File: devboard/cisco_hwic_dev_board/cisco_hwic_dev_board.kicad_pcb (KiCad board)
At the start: 2 copper layers, 3 parts, among them J1 Conn_02x20_Odd_Even, J2 Conn_02x34_Top_Bottom_Cisco, J3 Conn_01x15

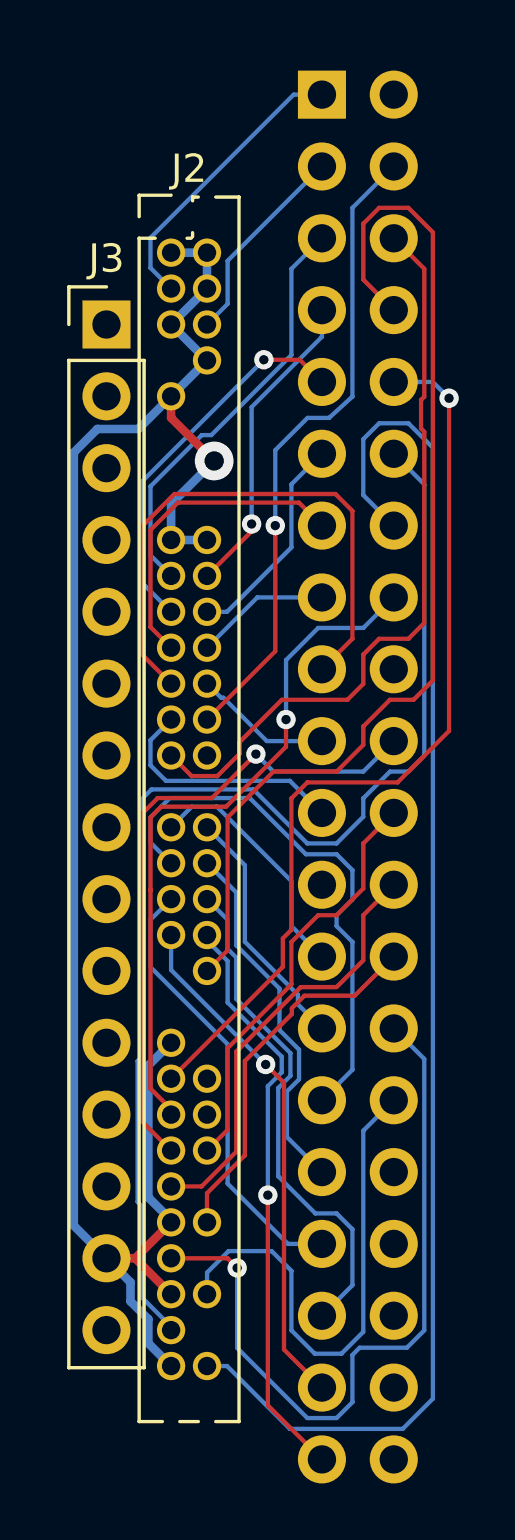
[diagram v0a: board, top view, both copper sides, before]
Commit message: Expansion connector routed.
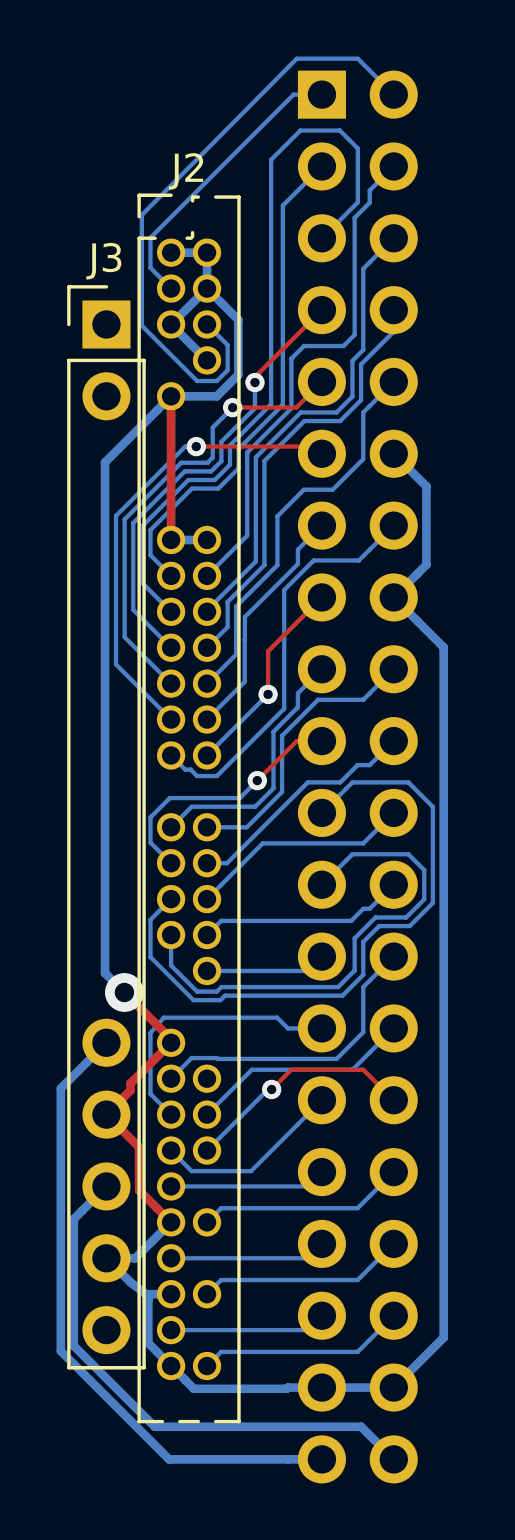
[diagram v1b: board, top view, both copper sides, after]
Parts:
- J3: footprint Connector_PinHeader_2.54mm:PinHeader_1x15_P2.54mm_Vertical -> cisco_hwic_dev_board:PinHeader_1x15_P2.54mm_Vertical_Cisco
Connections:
- J1 pad 10: /DCLK_OE_ -> /PB7
- J1 pad 11: /PB3 -> /PB8
- J1 pad 12: /PH0 -> GND
- J1 pad 13: /PB4 -> /PC0
- J1 pad 14: /PH1 -> /PC1
- J1 pad 15: /PB5 -> /PC2
- J1 pad 16: /PG0 -> GND
- J1 pad 17: /PB6 -> /PD0
- J1 pad 18: /PG1 -> /PD1
- J1 pad 19: /PB7 -> /PD2
- J1 pad 2: Net-(J1-Pad2) -> /PA1
- J1 pad 20: /PG2 -> /PD3
- J1 pad 21: /PB8 -> /PD4
- J1 pad 22: /PG3 -> /PD5
- J1 pad 23: Net-(J1-Pad23) -> /PD6
- J1 pad 24: /PG4 -> /PD7
- J1 pad 25: /PD0 -> /PE0
- J1 pad 26: /PG5 -> /DCLK_OE_
- J1 pad 27: /PD1 -> /PG0
- J1 pad 28: /PG6 -> /PG1
- J1 pad 29: /PD2 -> /PG2
- J1 pad 3: /PA1 -> /DATA0
- J1 pad 30: /PG7 -> /PG3
- J1 pad 31: /PD3 -> /PG4
- J1 pad 32: Net-(J1-Pad32) -> /PG5
- J1 pad 33: /PD4 -> /PG6
- J1 pad 34: Net-(J1-Pad34) -> /PG7
- J1 pad 35: /PD5 -> /PH0
- J1 pad 36: Net-(J1-Pad36) -> /PH1
- J1 pad 37: /PD6 -> GND
- J1 pad 38: Net-(J1-Pad38) -> GND
- J1 pad 39: /PD7 -> +5V
- J1 pad 4: /PC0 -> /PB1
- J1 pad 40: Net-(J1-Pad40) -> +3V3
- J1 pad 5: /DATA0 -> /PB2
- J1 pad 6: /PC1 -> /PB3
- J1 pad 7: /PB1 -> /PB4
- J1 pad 8: /PE0 -> /PB5
- J1 pad 9: /PB2 -> /PB6
- J2 pad 50: /Pin_50 -> /PC2
- J2 pad 60: Net-(J2-Pad60) -> /PG1
- J3 pad 11: Net-(J3-Pad11) -> +5V
- J3 pad 12: +5V -> GND
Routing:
- net /PH1: track 49.5 -> 7.34 mm
- net GND: track 65.2 -> 103.9 mm
- net /PH0: track 43.0 -> 5.54 mm
- net /PE0: track 37.8 -> 4.27 mm
- net +5V: track 0.00 -> 22.4 mm
- net /DCLK_OE_: track 32.2 -> 10.6 mm, vias 1 -> 0
- net /PG6: track 26.3 -> 5.54 mm, vias 1 -> 0
- net +3V3: track 0.00 -> 19.1 mm
- net /PG2: track 22.8 -> 6.67 mm, vias 1 -> 0
- net /PG0: track 24.5 -> 9.66 mm, vias 1 -> 0
- net /PA1: track 7.27 -> 21.6 mm
- net /PC0: track 22.8 -> 8.54 mm, vias 1 -> 0
- net /PD7: track 20.6 -> 7.34 mm, vias 1 -> 0
- net /PB2: track 13.5 -> 26.3 mm, vias 1 -> 0
- net /PC1: track 26.5 -> 14.3 mm
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
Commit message: First version.
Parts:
- added C1: C, Capacitor_SMD:C_0603_1608Metric_Pad1.05x0.95mm_HandSolder, F.Cu at (-551.3, -538.7)
- added C2: C, Capacitor_SMD:C_0603_1608Metric_Pad1.05x0.95mm_HandSolder, F.Cu at (-547.0, -564.4)
- added J4: USB Blaster Active Serial, Connector_PinHeader_2.54mm:PinHeader_2x05_P2.54mm_Vertical, B.Cu at (-551.9, -550.7)
- added J5: ATT85_VIN, Connector_PinHeader_2.54mm:PinHeader_1x01_P2.54mm_Vertical, B.Cu at (-554.5, -566.2)
- added J6: SD Card, Connector_PinHeader_2.54mm:PinHeader_1x06_P2.54mm_Vertical, B.Cu at (-554.5, -536.4)
- added J7: Power, Connector_PinHeader_2.54mm:PinHeader_1x03_P2.54mm_Horizontal, F.Cu at (-554.2, -579.6)
- added JP1: 3.3V Main, Connector_PinHeader_2.54mm:PinHeader_2x01_P2.54mm_Vertical, B.Cu at (-554.5, -561.8)
- added JP2: Jumper_3_Bridged12, Connector_PinHeader_2.54mm:PinHeader_1x03_P2.54mm_Vertical, B.Cu at (-554.2, -555.8)
- added R3: NS, Resistor_SMD:R_0603_1608Metric_Pad1.05x0.95mm_HandSolder, F.Cu at (-549.0, -578.6)
- added R4: NS, Resistor_SMD:R_0603_1608Metric_Pad1.05x0.95mm_HandSolder, F.Cu at (-545.5, -578.6)
- added R5: NS, Resistor_SMD:R_0603_1608Metric_Pad1.05x0.95mm_HandSolder, F.Cu at (-549.0, -580.1)
- added R6: NS, Resistor_SMD:R_0603_1608Metric_Pad1.05x0.95mm_HandSolder, F.Cu at (-545.5, -580.1)
- added R7: NS, Resistor_SMD:R_0603_1608Metric_Pad1.05x0.95mm_HandSolder, F.Cu at (-550.8, -581.9)
- added R8: NS, Resistor_SMD:R_0603_1608Metric_Pad1.05x0.95mm_HandSolder, F.Cu at (-545.5, -581.9)
- added U1: AT25xxx, Package_SO:SOIC-8_3.9x4.9mm_P1.27mm, F.Cu at (-548.5, -569.3)
- added U2: ATtiny85_devboard, cisco_hwic_dev_board:Digispark_ATtiny85, B.Cu at (-551.7, -584.7)
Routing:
- net GND: track 103.9 -> 211.8 mm, vias 1 -> 3
- net +3V3: track 19.1 -> 109.5 mm, vias 0 -> 2
- net /DCLK: track 0.00 -> 71.0 mm, vias 0 -> 3
- net /DATA0: track 17.8 -> 77.2 mm, vias 0 -> 2
- net /SPI_MISO: track 0.00 -> 58.3 mm, vias 0 -> 1
- net /DCLK_OE_: track 10.6 -> 64.9 mm
- net +5V: track 22.4 -> 73.9 mm
- net /SPISD_CSN: track 0.00 -> 32.2 mm
- net /PC1: track 14.3 -> 41.1 mm
- net /SPI_CSN: track 0.00 -> 26.4 mm
- net /PC0: track 8.54 -> 34.6 mm, vias 0 -> 2
- net /SD_CSN: track 0.00 -> 22.1 mm
- net Net-(J5-Pad1): track 0.00 -> 12.3 mm
- net Net-(JP1-Pad1): track 0.00 -> 11.0 mm
- net Net-(R8-Pad2): track 0.00 -> 6.77 mm
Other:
- board outline added: 27.4 x 52.1 mm
- board text added: "3.3V"
- board text added: "5V"
- board text added: "DCLK"
- board text added: "GND"
- board text added: "MISO"
- board text added: "MOSI"
- board text added: "PA0"
- board text added: "PB0"
- board text added: "PC0"
- board text added: "PD0"
- board text added: "PE0"
- board text added: "PG0"
- board text added: "PH0"

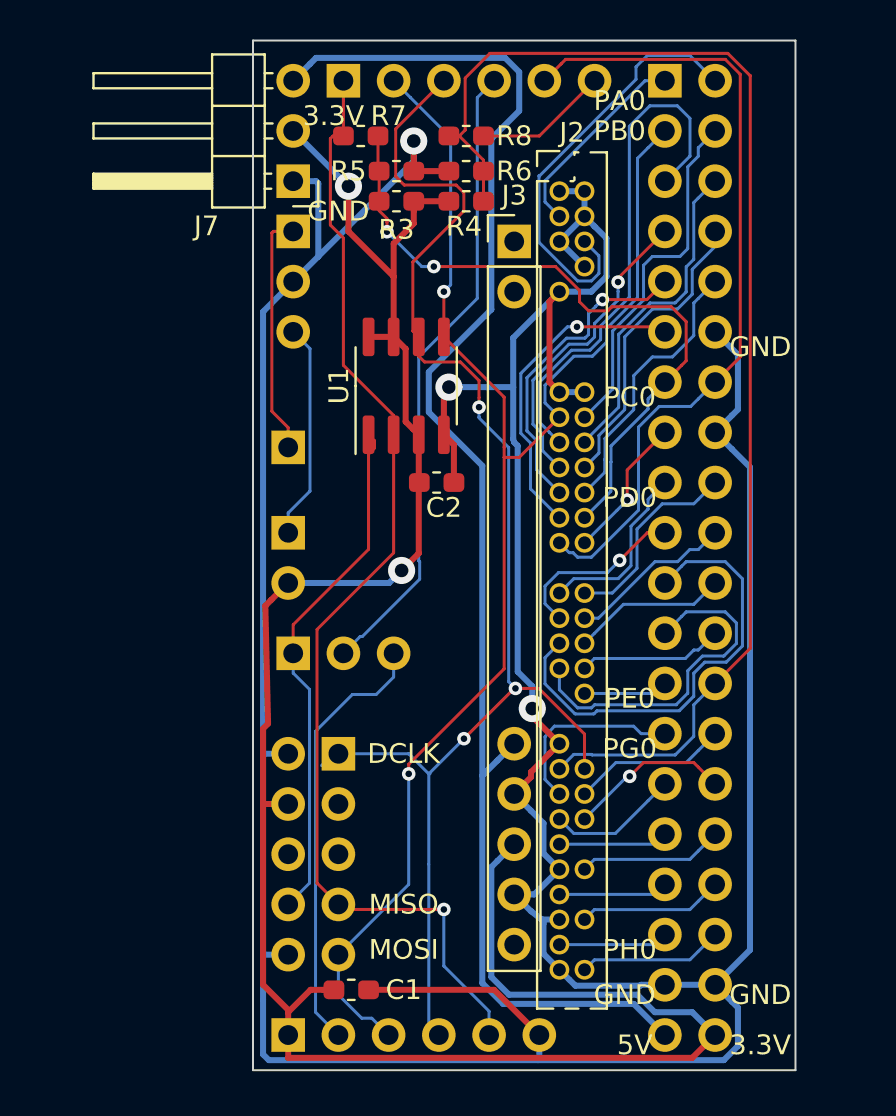
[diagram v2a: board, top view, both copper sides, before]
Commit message: Various fixes after broken rev 1.
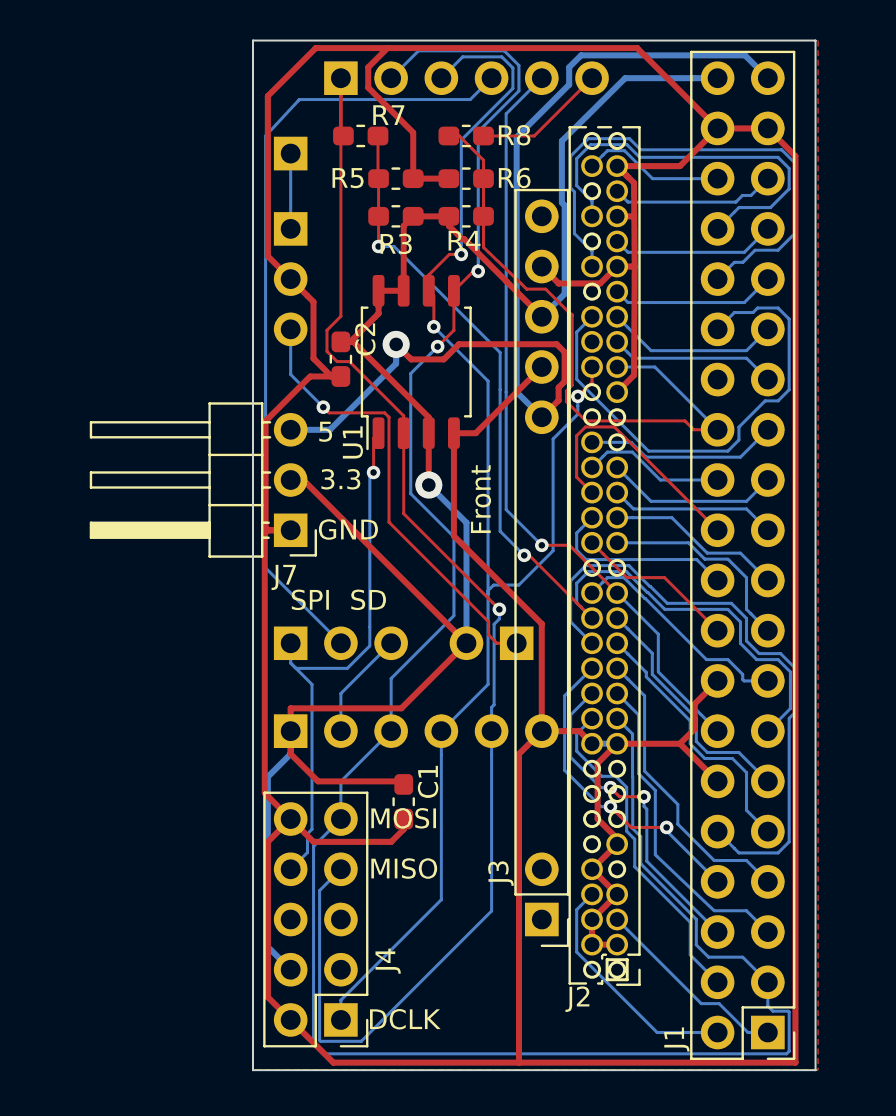
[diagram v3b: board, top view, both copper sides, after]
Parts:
- J1: footprint Connector_PinSocket_2.54mm:PinSocket_2x20_P2.54mm_Horizontal -> Connector_PinHeader_2.54mm:PinHeader_2x20_P2.54mm_Vertical; moved to F.Cu
- J4: moved to F.Cu
- U1: footprint Package_SO:SOIC-8_3.9x4.9mm_P1.27mm -> Package_SO:SOIC-8_5.275x5.275mm_P1.27mm
- moved J1 48.4 mm to (-530.2, -536.6)
- moved J2 40.7 mm to (-537.8, -539.8), turned to 180 degrees
- moved J3 34.3 mm to (-541.7, -542.3), turned to 180 degrees
- moved J7 17.7 mm to (-554.4, -562.0)
- moved J6 15.4 mm to (-554.4, -551.8)
- moved J5 14.9 mm to (-554.4, -581.0)
- moved J4 13.5 mm to (-551.8, -537.2)
- moved JP1 12.8 mm to (-542.9, -556.3), turned to 180 degrees
- moved C1 9.87 mm to (-548.6, -548.2), turned to 270 degrees
- moved C2 7.89 mm to (-551.8, -570.6), turned to 270 degrees
- moved U1 1.31 mm to (-548.0, -570.5)
- moved R3 0.76 mm to (-549.0, -577.9)
- moved R4 0.76 mm to (-545.5, -577.9)
- moved JP2 0.52 mm to (-554.4, -556.3)
- moved R5 0.38 mm to (-549.0, -579.8)
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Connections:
- J2 pad 60: /PG1 -> Net-(J2-Pad60)
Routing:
- net GND: track 211.8 -> 266.2 mm, vias 3 -> 0
- net /DCLK_OE_: track 64.9 -> 31.7 mm
- net /DATA0: track 77.2 -> 109.3 mm
- net +5V: track 73.9 -> 50.9 mm, vias 0 -> 1
- net /PG5: track 7.34 -> 26.7 mm
- net /PB7: track 14.0 -> 31.4 mm
- net /PG3: track 8.23 -> 25.3 mm, vias 1 -> 0
- net /SD_CSN: track 22.1 -> 5.50 mm
- net /PD4: track 23.2 -> 8.41 mm
- net /PC0: track 34.6 -> 48.8 mm
- net /PG7: track 7.34 -> 20.3 mm
- net Net-(JP1-Pad1): track 11.0 -> 22.8 mm, vias 0 -> 1
- net /SPI_MISO: track 58.3 -> 70.1 mm
- net +3V3: track 109.5 -> 99.0 mm, vias 2 -> 1
- net /PB2: track 26.3 -> 16.2 mm
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- added copper zone on F.Cu, net GND
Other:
- board size 27.4 x 52.1 mm -> 28.4 x 52.1 mm
- board text added: "3.3"
- board text added: "5"
- board text added: "Back"
- board text added: "Front"
- board text added: "HWIC DevBoard Tom Verbeure"
- board text added: "SD"
- board text added: "SDcard"
- board text added: "SPI"
- board text removed: "3.3V"
- board text removed: "5V"
- board text removed: "PA0"
- board text removed: "PB0"
- board text removed: "PC0"
- board text removed: "PD0"
- board text removed: "PE0"
- board text removed: "PG0"
- board text removed: "PH0"

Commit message: Move ATtiny and SDcard for accessibility while soldered down.
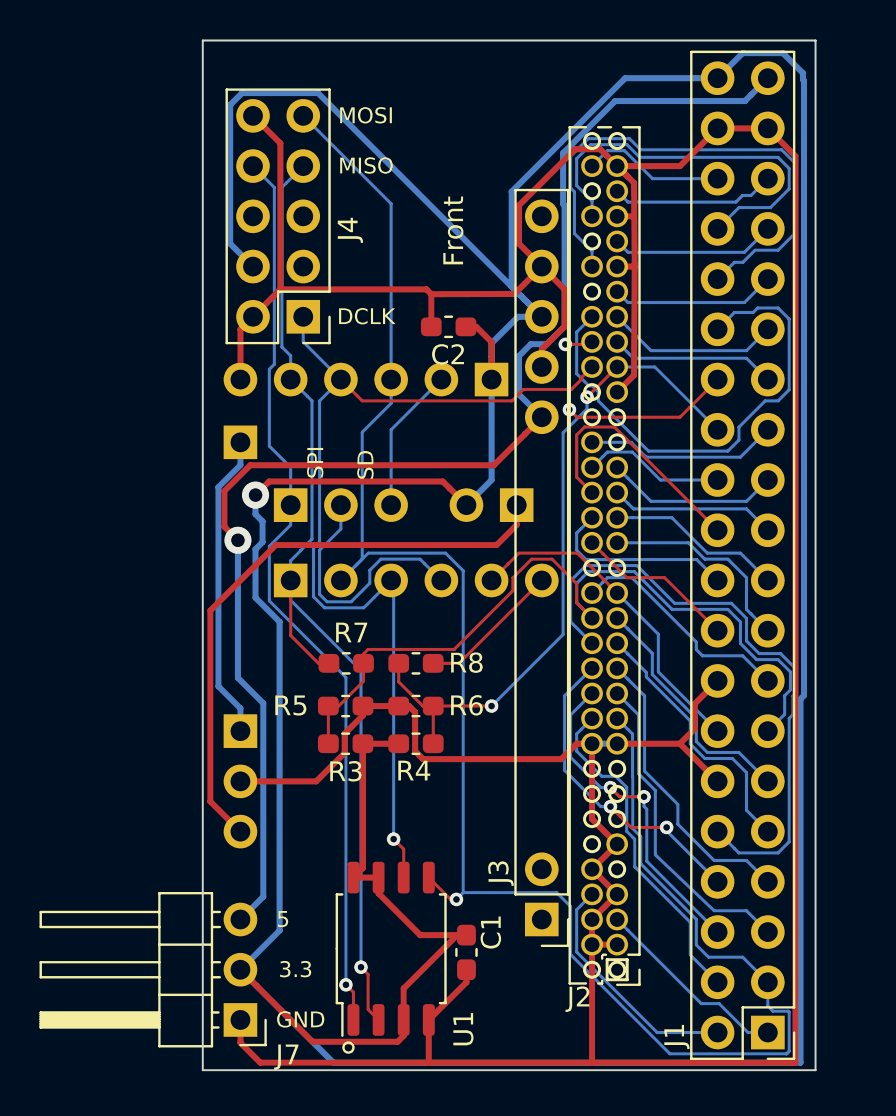
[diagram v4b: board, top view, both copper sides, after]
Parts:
- moved J4 35.6 mm to (-553.7, -572.8)
- moved U1 29.7 mm to (-549.3, -540.8)
- moved R3 26.8 mm to (-551.6, -551.2)
- moved R4 26.8 mm to (-548.0, -551.2)
- moved R5 26.8 mm to (-551.6, -553.1)
- moved R6 26.8 mm to (-548.0, -553.1)
- moved R8 26.8 mm to (-548.0, -555.2)
- moved R7 26.7 mm to (-551.5, -555.2)
- moved U2 25.5 mm to (-554.4, -559.4)
- moved J7 24.9 mm to (-556.9, -537.2)
- moved J6 20.5 mm to (-544.2, -569.6), turned to 90 degrees
- moved J5 14.8 mm to (-556.9, -566.4)
- moved C1 8.25 mm to (-545.5, -540.6)
- moved JP1 6.99 mm to (-542.9, -563.2)
- moved JP2 6.99 mm to (-554.4, -563.2)
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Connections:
- net Net-(J5-Pad1) renamed +8V
- net Net-(JP1-Pad1) renamed VDD
- J2 pad 60: Net-(J2-Pad60) -> /PG1
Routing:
- net +3V3: track 99.0 -> 219.9 mm
- net GND: track 266.2 -> 206.1 mm
- net /SPISD_CSN: track 39.9 -> 13.0 mm
- net /DCLK: track 73.3 -> 49.4 mm, vias 3 -> 1
- net /PC1: track 39.0 -> 17.2 mm, vias 1 -> 0
- net /SPI_CSN: track 27.8 -> 46.4 mm
- net /SPI_MISO: track 70.1 -> 51.8 mm
- net +5V: track 50.9 -> 67.8 mm
- net /DATA0: track 109.3 -> 95.5 mm, vias 2 -> 1
- net /PG1: track 0.00 -> 13.2 mm, vias 0 -> 2
- net +8V: track 3.81 -> 15.5 mm
- net /PC0: track 48.8 -> 40.7 mm, vias 2 -> 0
- net VDD: track 22.8 -> 30.1 mm, vias 1 -> 0
- net /DCLK_OE_: track 31.7 -> 34.2 mm, vias 0 -> 2
- net /SD_CSN: track 5.50 -> 7.40 mm
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- removed copper zone on F.Cu, net GND
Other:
- board size 28.4 x 52.1 mm -> 31 x 52.1 mm
- board text added: "3.3V"
- board text added: "CSN"
- board text added: "DATA0"
- board text added: "DCLK_OE_"
- board text added: "VDD"
- board text added: "VIN"
- board text added: "nCONFIG"

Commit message: Remove 2 resistors. Connect AT_PB5.
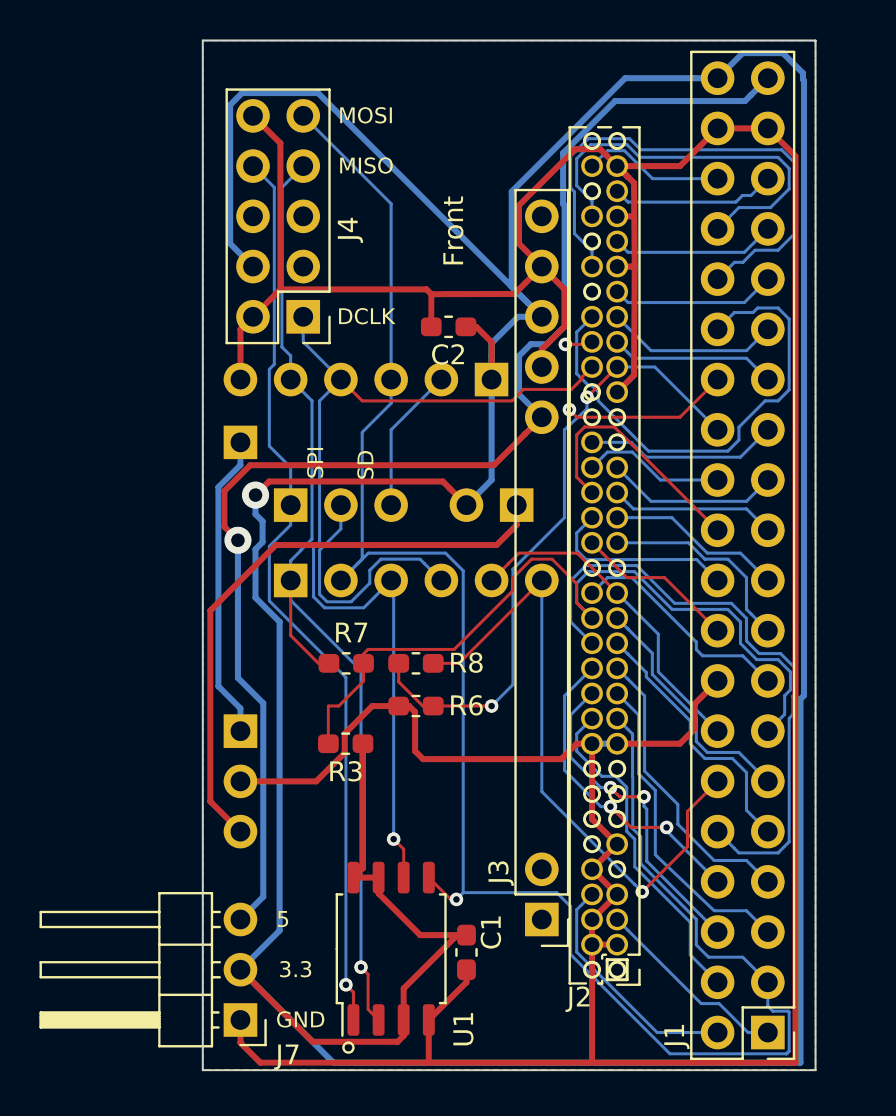
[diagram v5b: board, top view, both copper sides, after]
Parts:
- removed R4, R5: NS, Resistor_SMD:R_0603_1608Metric_Pad1.05x0.95mm_HandSolder
- R3, R6: value NS -> 10K
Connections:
- net /DCLK_OE_ renamed /DCLK_ALT
- J1 pad 12: GND -> /AT_PB5
- R8 pad 2: Net-(R8-Pad2) -> /AT_PB5
- U2 pad 6: Net-(R8-Pad2) -> /AT_PB5
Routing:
- net /AT_PB5: track 0.00 -> 32.2 mm, vias 0 -> 1
- net Net-(R8-Pad2): track 7.22 -> 0.00 mm
- net GND: track 206.1 -> 203.2 mm
- net /DCLK_ALT: track 34.2 -> 32.3 mm
- net +3V3: track 219.9 -> 218.1 mm
- added copper zone on B.Cu, net +3V3
- added copper zone on F.Cu, net GND
